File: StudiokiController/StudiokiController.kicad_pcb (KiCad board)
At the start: 2 copper layers, 23 parts, among them J1 USB_B_Mini, J2 Conn_01x30_Male, Q1 Q_DUAL_NPN_NPN_E1B1C2E2B2C1, U1 CH340G, U2 ESP32-WROOM-32D

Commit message: Added MAX31855
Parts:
- added C12: 0.1uF, Capacitor_SMD:C_0603_1608Metric, F.Cu at (124.7, 143.8)
- added J3: Conn_01x04_Male, Connector_PinHeader_2.54mm:PinHeader_1x04_P2.54mm_Vertical, F.Cu at (120.4, 135.8)
- added J4: 57PC5FS, StudiokiController:57PC5FS, F.Cu at (101.3, 144.3)
- added J5: Conn_01x02_Female, TerminalBlock:TerminalBlock_bornier-2_P5.08mm, F.Cu at (125.9, 138.0)
- added R10: 100, Resistor_SMD:R_0603_1608Metric, F.Cu at (128.7, 143.8)
- added R11: 100, Resistor_SMD:R_0603_1608Metric, F.Cu at (128.5, 146.3)
- added R8: 100, Resistor_SMD:R_0603_1608Metric, F.Cu at (136.3, 134.7)
- added R9: 100, Resistor_SMD:R_0603_1608Metric, F.Cu at (120.1, 153.4)
- added U3: MAX31855KASA, Package_SO:SOIC-8_3.9x4.9mm_P1.27mm, F.Cu at (122.3, 148.9)
- U1: value CH340G -> CH340C
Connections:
- J2 pad 14: DISPLAY -> DISP_RES
- U2 pad 13: DISPLAY -> MTMS
- U2 pad 14: Net-(U2-Pad14) -> MTDI
- U2 pad 16: Net-(U2-Pad16) -> MTCK
- U2 pad 18: Net-(U2-Pad18) -> SPI_SCK
- U2 pad 19: Net-(U2-Pad19) -> SPI_MISO
- U2 pad 23: SW1 -> MTDO
- U2 pad 26: Net-(U2-Pad26) -> DISP_RES
- U2 pad 27: SW2 -> Net-(U2-Pad27)
- U2 pad 28: SW3 -> SW1
- U2 pad 29: Net-(U2-Pad29) -> SPI_SS
- U2 pad 30: Net-(U2-Pad30) -> SW2
- U2 pad 31: Net-(U2-Pad31) -> SW3

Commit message: added several Parts
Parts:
- added D1: LED, LED_SMD:LED_0603_1608Metric, F.Cu at (93.5, 106.2)
- added D2: 1N4148W-TP, Diode_SMD:D_SOD-123, F.Cu at (90.5, 105.3)
- added D3: LED, LED_SMD:LED_0603_1608Metric, F.Cu at (89.5, 91.9)
- added D4: 1N4148W-TP, Diode_SMD:D_SOD-123, F.Cu at (90.3, 88.9)
- added F1: Fuse, StudiokiController:Littelfuse65800001009, F.Cu at (108.0, 54.6)
- added J6: Screw_Terminal_01x03, WJ142R-5.08-3P:RHDR6W120P762X508_2X3_1524X1410X1355P, F.Cu at (123.2, 55.9)
- added J7: WJ142R-5.08-3P, StudiokiController:RHDR6W120P762X508_2X3_1524X1410X1355P, F.Cu at (121.9, 83.8)
- added PS1: RAC03-12SK, RAC03-12SK:CONV_RAC03-12SK, F.Cu at (104.1, 71.1)
- added Q2: PMV20XNE, Package_TO_SOT_SMD:SOT-23, F.Cu at (91.1, 100.2)
- added Q3: PMV20XNE, Package_TO_SOT_SMD:SOT-23, F.Cu at (95.4, 89.5)
- added R12: 10k, Resistor_SMD:R_0603_1608Metric, F.Cu at (94.6, 102.2)
- added R13: 10k, Resistor_SMD:R_0603_1608Metric, F.Cu at (93.5, 93.0)
- added RLA1: OJE-SH-112HM_000, StudiokiController:OJE-SH-112HM_000, F.Cu at (100.3, 105.4)
- added RLA2: OJE-SH-112HM_000, StudiokiController:OJE-SH-112HM_000, F.Cu at (100.3, 94.0)
- added SW1: SW_Push, StudiokiController:TSA063G50250, F.Cu at (56.5, 101.0)
- added SW2: SW_Push, StudiokiController:TSA063G50250, F.Cu at (56.5, 109.2)
- added SW3: SW_Push, StudiokiController:TSA063G50250, F.Cu at (56.5, 92.7)
- moved J1 78.8 mm to (63.8, 53.9), turned to 180 degrees
- moved J5 55.7 mm to (79.2, 107.7), turned to 180 degrees
- moved U1 53.4 mm to (74.9, 57.8)
- moved U2 45.1 mm to (65.4, 74.9), turned to 90 degrees
- moved C1 43.3 mm to (161.5, 68.8)
- moved C4 43.3 mm to (161.5, 66.3)
- moved C5 43.3 mm to (165.6, 63.8)
- moved R1 43.3 mm to (163.8, 77.0)
- moved R2 43.3 mm to (157.1, 72.8)
- moved R3 43.3 mm to (161.5, 63.8)
- moved R4 43.3 mm to (165.6, 61.3)
- moved R6 43.3 mm to (161.5, 61.3)
- moved C2 43.3 mm to (153.1, 72.8)
- moved C3 43.3 mm to (153.1, 77.8)
- moved R5 43.3 mm to (153.1, 75.3)
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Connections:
- U2 pad 11: Net-(U2-Pad11) -> RELAY1
- U2 pad 12: Net-(U2-Pad12) -> RELAY2
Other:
- board outline added: 85 x 65 mm

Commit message: first PCB
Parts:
- removed R10, R11, R9: 100, Resistor_SMD:R_0603_1608Metric
- added C10: 100nF, Capacitor_SMD:C_0603_1608Metric, F.Cu at (58.3, 62.9)
- added C13: 100nF, Capacitor_SMD:C_0603_1608Metric, F.Cu at (61.4, 118.4)
- added C19: 1uF, Capacitor_SMD:C_0603_1608Metric, F.Cu at (56.9, 99.2)
- added C6: 100nF, Capacitor_SMD:C_0603_1608Metric, F.Cu at (58.6, 97.2)
- added C7: 100nF, Capacitor_SMD:C_0603_1608Metric, F.Cu at (93.0, 70.4)
- added C8: 10uF tantal, Capacitor_Tantalum_SMD:CP_EIA-3216-12_Kemet-S, F.Cu at (92.5, 72.6)
- added C9: 10uF tantal, Capacitor_Tantalum_SMD:CP_EIA-3216-12_Kemet-S, F.Cu at (87.1, 66.3)
- added D5: LED, LED_SMD:LED_0603_1608Metric, F.Cu at (66.7, 87.7)
- added D6: LED, LED_SMD:LED_0603_1608Metric, F.Cu at (68.5, 87.7)
- added D7: LED, LED_SMD:LED_0603_1608Metric, F.Cu at (64.9, 87.7)
- added D8: LED, LED_SMD:LED_0603_1608Metric, F.Cu at (97.6, 117.2)
- added D9: 1N4148W-TP, Diode_SMD:D_SOD-123, F.Cu at (105.7, 115.5)
- added J2: WJ142R-5.08-3P, StudiokiController:RHDR6W120P762X508_2X3_1524X1410X1355P, F.Cu at (137.2, 105.7)
- added J8: Conn_01x04_Female, Connector_PinHeader_2.54mm:PinHeader_1x04_P2.54mm_Vertical, F.Cu at (65.9, 96.4)
- added J9: Conn_01x04_Female, Connector_PinHeader_2.54mm:PinHeader_1x04_P2.54mm_Vertical, F.Cu at (61.2, 96.4)
- added Q4: PMV20XNE, Package_TO_SOT_SMD:SOT-23, F.Cu at (102.2, 117.2)
- added RLA3: OJE-SH-112HM_000, StudiokiController:OJE-SH-112HM_000, F.Cu at (108.7, 118.9)
- added U4: AZ1117-3.3, Package_TO_SOT_SMD:SOT-223, F.Cu at (91.9, 64.5)
- C11: value 1uF -> 100nF
- C12: value 0.1uF -> 100nF
- J3: value Conn_01x04_Male -> Conn_01x04_Female
- J6: value Screw_Terminal_01x03 -> WJ142R-5.08-3P; footprint WJ142R-5.08-3P:RHDR6W120P762X508_2X3_1524X1410X1355P -> StudiokiController:RHDR6W120P762X508_2X3_1524X1410X1355P
- R8: value 100 -> 10k
- SW1, SW2, SW3: footprint StudiokiController:TSA063G50250 -> Button_Switch_SMD:SW_SPST_PTS645
- moved C5 109.5 mm to (58.8, 88.0), turned to 180 degrees
- moved C11 105.6 mm to (54.3, 118.5), turned to 180 degrees
- moved C15 105.5 mm to (55.8, 109.9)
- moved C14 105.3 mm to (55.8, 111.5)
- moved C4 104.7 mm to (58.8, 86.2), turned to 180 degrees
- moved R3 99.9 mm to (61.6, 63.5), turned to 90 degrees
- moved C16 98.9 mm to (55.7, 96.0), turned to 180 degrees
- moved C2 95.9 mm to (58.8, 89.7), turned to 180 degrees
- moved C18 95.6 mm to (55.3, 99.2), turned to 270 degrees
- moved C17 95.1 mm to (55.5, 92.7), turned to 180 degrees
- moved R2 94.3 mm to (63.3, 63.5), turned to 90 degrees
- moved C1 90.9 mm to (71.5, 56.2)
- moved R4 87.5 mm to (78.1, 57.7), turned to 270 degrees
- moved R1 84.7 mm to (80.8, 60.5)
- moved R6 82.9 mm to (78.8, 66.3)
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- renumbered C6 to C14, C7 to C15, C8 to C16, C9 to C17, C10 to C18, J2 to J10
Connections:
- C11 pad 1: +3V3 -> GND
- C11 pad 2: Net-(C10-Pad2) -> SW2
- C18 pad 2: Net-(C10-Pad2) -> GND
- D2 pad 1: Net-(D2-Pad1) -> +12V
- D4 pad 1: Net-(D4-Pad1) -> +12V
- J3 pad 1: Net-(J3-Pad1) -> GND
- J3 pad 2: Net-(J3-Pad2) -> +3V3
- J3 pad 3: Net-(J3-Pad3) -> SCL
- J3 pad 4: Net-(J3-Pad4) -> SDA
- J5 pad 1: Net-(J4-Pad1) -> Net-(J4-Pad3)
- J5 pad 2: Net-(J4-Pad2) -> Net-(J4-Pad1)
- J6 pad 1: Net-(J6-Pad1) -> Net-(F1-Pad2)
- J6 pad 2: 230V-N -> Net-(F1-Pad2)
- J6 pad 3: Net-(F1-Pad2) -> 230V-N
- J6 pad 4: (no net) -> 230V-N
- J6 pad 5: (no net) -> PE
- J6 pad 6: (no net) -> PE
- J7 pad 2: Net-(J7-Pad2) -> 230V-N
- J7 pad 4: Net-(J7-Pad4) -> /230V-Relay/OUTPUT-A
- J7 pad 5: Net-(J7-Pad5) -> PE
- J7 pad 6: Net-(J7-Pad6) -> PE
- R8 pad 1: MTMS -> RELAY3
- R8 pad 2: Net-(J3-Pad1) -> GND
- U2 pad 1: Net-(U2-Pad1) -> GND
- U2 pad 10: Net-(U2-Pad10) -> RELAY3
- U2 pad 13: MTMS -> Net-(U2-Pad13)
- U2 pad 14: MTDI -> Net-(U2-Pad14)
- U2 pad 15: Net-(U2-Pad1) -> GND
- U2 pad 16: MTCK -> SCL
- U2 pad 17: Net-(U2-Pad17) -> SDA
- U2 pad 23: MTDO -> Net-(U2-Pad23)
- U2 pad 28: SW1 -> Net-(U2-Pad28)
- U2 pad 36: SCL -> Net-(U2-Pad36)
- U2 pad 37: SDA -> SW1
- U2 pad 38: Net-(U2-Pad1) -> GND
- U2 pad 7: Net-(U2-Pad7) -> LED3
- U2 pad 8: Net-(U2-Pad8) -> LED1
- U2 pad 9: Net-(U2-Pad9) -> LED2
- U3 pad 2: Net-(J4-Pad1) -> Net-(J4-Pad3)
- U3 pad 3: Net-(J4-Pad2) -> Net-(J4-Pad1)
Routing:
- net +3V3: track 0.00 -> 137.3 mm, vias 0 -> 4
- net 230V-N: track 0.00 -> 75.7 mm
- net +12V: track 0.00 -> 74.8 mm
- net PE: track 0.00 -> 73.1 mm
- net SW2: track 0.00 -> 71.8 mm, vias 0 -> 2
- net 230V-L: track 0.00 -> 70.6 mm
- net GND: track 0.00 -> 65.4 mm, vias 0 -> 18
- net SW3: track 0.00 -> 65.3 mm, vias 0 -> 2
- net RELAY3: track 0.00 -> 59.7 mm
- net SPI_SS: track 0.00 -> 51.6 mm, vias 0 -> 2
- net SDA: track 0.00 -> 50.8 mm, vias 0 -> 2
- net DISP_RES: track 0.00 -> 49.2 mm, vias 0 -> 2
- net EN: track 0.00 -> 48.7 mm, vias 0 -> 2
- net SCL: track 0.00 -> 46.6 mm, vias 0 -> 2
- net RELAY1: track 0.00 -> 46.5 mm
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- added copper zone on B.Cu, net GND
- added copper zone on F.Cu, net GND
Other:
- board size 85 x 65 mm -> 100 x 80 mm
- board text added: "PE"

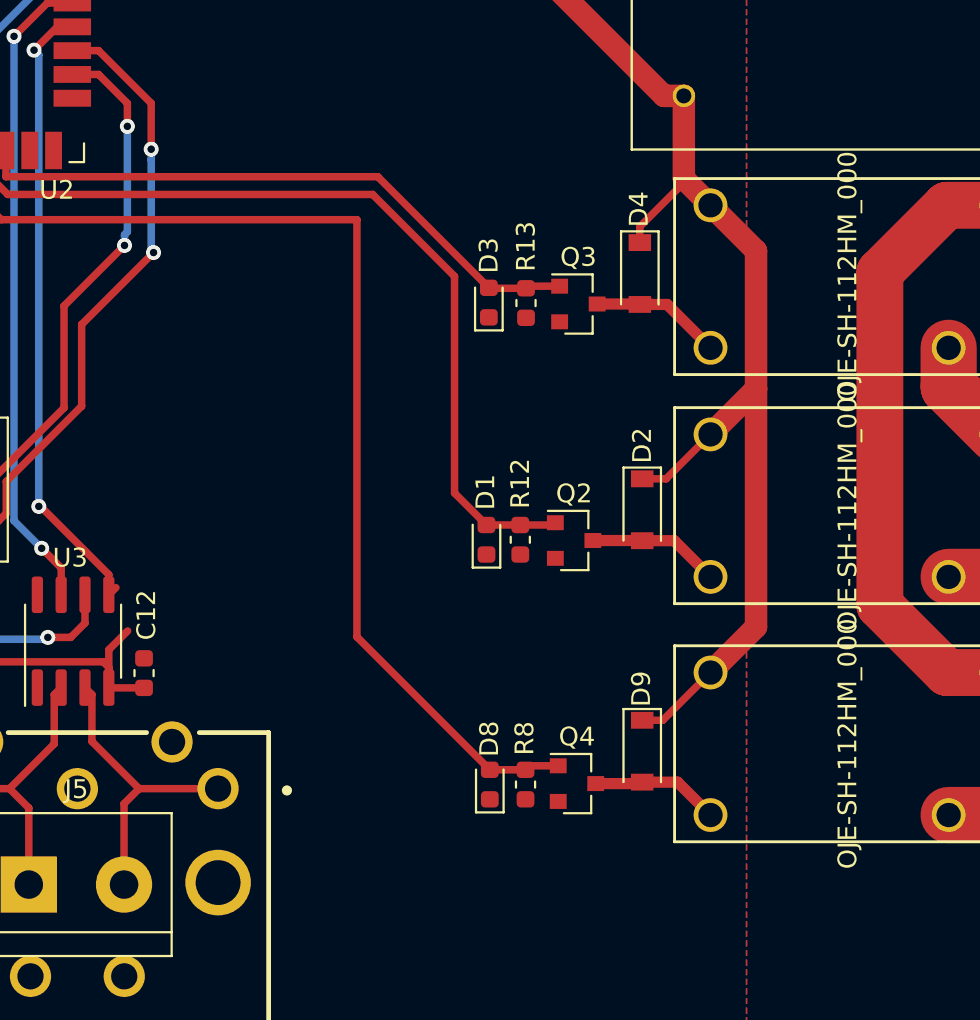
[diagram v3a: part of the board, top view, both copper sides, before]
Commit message: changed silkscreen
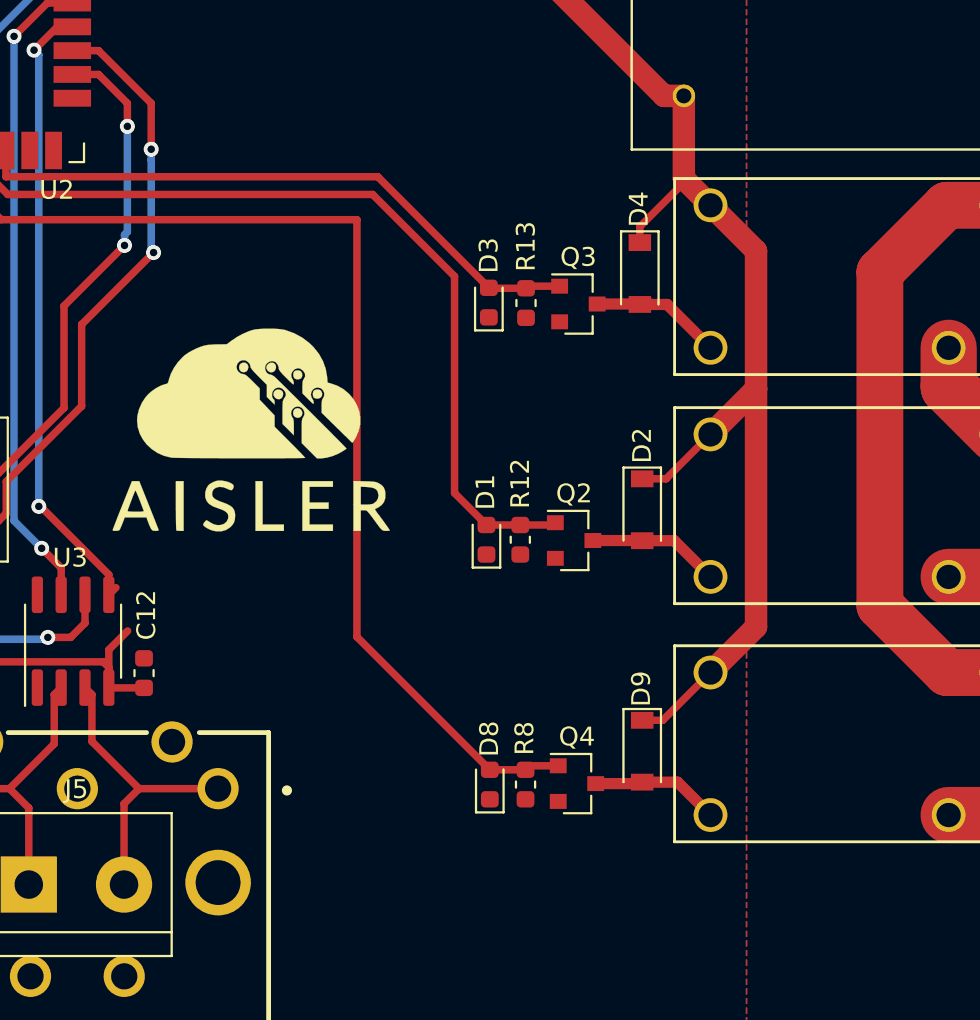
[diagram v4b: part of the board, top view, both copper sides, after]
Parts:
- added G***: LOGO, StudiokiController:Aisler_Logo, F.Cu at (84.8, 98.3)

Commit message: New Layout
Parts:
- removed C14: 2.2uF, Capacitor_SMD:C_0603_1608Metric
- removed C15: 4.7uF, Capacitor_SMD:C_0603_1608Metric
- removed C16, C17, C18, C19: 1uF, Capacitor_SMD:C_0603_1608Metric
- added H1: MountingHole, MountingHole:MountingHole_3.2mm_M3_Pad_Via, F.Cu at (186.8, 66.4)
- added H2: MountingHole, MountingHole:MountingHole_3.2mm_M3_Pad_Via, F.Cu at (186.8, 115.7)
- added H3: MountingHole, MountingHole:MountingHole_3.2mm_M3_Pad_Via, F.Cu at (267.3, 66.4)
- added H4: MountingHole, MountingHole:MountingHole_3.2mm_M3_Pad_Via, F.Cu at (267.3, 115.7)
- added J11: Screw_Terminal_01x03, TerminalBlock_Phoenix:TerminalBlock_Phoenix_PT-1,5-3-5.0-H_1x03_P5.00mm_Horizontal, F.Cu at (244.6, 53.3)
- added J12: Screw_Terminal_01x02, TerminalBlock_Phoenix:TerminalBlock_Phoenix_PT-1,5-2-5.0-H_1x02_P5.00mm_Horizontal, F.Cu at (264.6, 53.3)
- added R10: 100, Resistor_SMD:R_0603_1608Metric, F.Cu at (245.7, 118.8)
- added R9: 100, Resistor_SMD:R_0603_1608Metric, F.Cu at (245.7, 115.3)
- added RV1: MOV-07D391KTR, Varistor:RV_Disc_D7mm_W4.5mm_P5mm, F.Cu at (199.4, 66.0)
- J10: value Conn_01x30_Male -> Conn_01x10_Male; footprint StudiokiController:OLED-solder -> Connector_IDC:IDC-Header_2x05_P2.54mm_Vertical
- J2, J6, J7: value WJ142R-5.08-3P -> Screw_Terminal_01x03; footprint StudiokiController:RHDR6W120P762X508_2X3_1524X1410X1355P -> TerminalBlock_Phoenix:TerminalBlock_Phoenix_PT-1,5-3-5.0-H_1x03_P5.00mm_Horizontal
- J3, J8, J9: footprint Connector_PinHeader_2.54mm:PinHeader_1x04_P2.54mm_Vertical -> Connector_PinSocket_2.54mm:PinSocket_1x04_P2.54mm_Vertical
- R7: value 910K -> 100
- moved J4 203.4 mm to (276.9, 101.2), turned to 180 degrees
- moved C6 197.3 mm to (253.6, 127.6), turned to 180 degrees
- moved J5 197.2 mm to (269.3, 103.8), turned to 90 degrees
- moved J9 193.7 mm to (252.8, 125.0), turned to 90 degrees
- moved R7 190.1 mm to (245.7, 117.0), turned to 180 degrees
- moved J8 188.4 mm to (252.8, 119.9), turned to 90 degrees
- moved C5 187.0 mm to (242.0, 125.3), turned to 270 degrees
- moved C4 185.6 mm to (240.2, 125.3), turned to 270 degrees
- moved C2 184.3 mm to (240.2, 122.0), turned to 90 degrees
- moved J3 183.2 mm to (252.8, 114.8), turned to 90 degrees
- moved U3 181.1 mm to (256.3, 101.4), turned to 180 degrees
- moved D7 180.3 mm to (242.5, 118.8), turned to 180 degrees
- moved C12 179.4 mm to (258.0, 97.6), turned to 180 degrees
- moved D5 178.2 mm to (242.5, 117.0), turned to 180 degrees
- moved D6 176.2 mm to (242.5, 115.2), turned to 180 degrees
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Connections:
- D5 pad 1: GND -> Net-(D5-Pad1)
- D6 pad 1: GND -> Net-(D6-Pad1)
- D7 pad 1: GND -> Net-(D7-Pad1)
- J10 pad 1: GND -> +3V3
- J10 pad 10: GND -> SW3
- J10 pad 2: Net-(C17-Pad2) -> EN
- J10 pad 3: Net-(C17-Pad1) -> IO0
- J10 pad 4: Net-(C16-Pad1) -> IO2
- J10 pad 5: Net-(C16-Pad2) -> SCL
- J10 pad 6: +3V3 -> SDA
- J10 pad 7: Net-(J10-Pad7) -> SW1
- J10 pad 8: GND -> SW2
- J10 pad 9: +3V3 -> GND
- J2 pad 1: 230V-N -> PE
- J2 pad 2: 230V-N -> Net-(F1-Pad2)
- J2 pad 3: /sheet5DF376A8/OUTPUT-A -> 230V-N
- J6 pad 1: Net-(F1-Pad2) -> Net-(J6-Pad1)
- J6 pad 2: Net-(F1-Pad2) -> /230V-Relay/OUTPUT-B
- J6 pad 3: 230V-N -> /230V-Relay/OUTPUT-A
- J7 pad 1: 230V-N -> Net-(J7-Pad1)
- J7 pad 2: 230V-N -> /sheet5DF55D65/OUTPUT-B
- J7 pad 3: /230V-Relay/OUTPUT-A -> /sheet5DF55D65/OUTPUT-A
- R7 pad 1: Net-(J10-Pad26) -> GND
- R7 pad 2: GND -> Net-(D5-Pad1)
- RLA1 pad 1: /sheet5DF55D65/OUTPUT-A -> /230V-Relay/OUTPUT-B
- RLA2 pad 1: 230V-L -> /sheet5DF55D65/OUTPUT-B
- RLA3 pad 1: 230V-L -> /sheet5DF376A8/OUTPUT-B
- U2 pad 11: RELAY1 -> RELAY2
- U2 pad 12: RELAY2 -> RELAY1
- U2 pad 14: Net-(U2-Pad14) -> DOOR
- U2 pad 24: Net-(U2-Pad24) -> IO2
- U2 pad 26: DISP_RES -> SW1
- U2 pad 27: Net-(U2-Pad27) -> SW2
- U2 pad 28: Net-(U2-Pad28) -> SW3
- U2 pad 30: SW2 -> Net-(U2-Pad30)
- U2 pad 31: SW3 -> Net-(U2-Pad31)
- U2 pad 37: SW1 -> Net-(U2-Pad37)
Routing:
- net DOOR: track 0.00 -> 77.1 mm, vias 0 -> 2
- net PE: track 73.1 -> 0.00 mm
- net 230V-L: track 70.6 -> 8.20 mm
- net SW1: track 15.6 -> 74.7 mm, vias 0 -> 1
- net 230V-N: track 75.7 -> 23.2 mm
- net DISP_RES: track 49.2 -> 0.00 mm, vias 2 -> 0
- net GND: track 65.4 -> 24.1 mm, vias 18 -> 12
- net +12V: track 74.8 -> 100.5 mm
- net SCL: track 46.6 -> 67.9 mm, vias 2 -> 1
- net SDA: track 50.8 -> 71.4 mm, vias 2 -> 1
- net /230V-Relay/OUTPUT-A: track 33.5 -> 13.9 mm
- net IO2: track 0.00 -> 15.5 mm
- net RELAY3: track 59.7 -> 45.4 mm, vias 0 -> 2
- net +3V3: track 137.3 -> 123.5 mm, vias 4 -> 6
- net IO0: track 13.6 -> 26.8 mm, vias 0 -> 2
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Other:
- board size 100 x 80 mm -> 100 x 85 mm
- board text added: "3V3"
- board text added: "EN"
- board text added: "GND"
- board text added: "IO0"
- board text added: "IO2"
- board text added: "Jan² 12-2019"
- board text added: "L"
- board text added: "N"
- board text added: "SCL"
- board text added: "SDA"
- board text added: "SW1"
- board text added: "SW2"
- board text added: "SW3"
- board text added: "Studioki Controll"

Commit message: changed parameters
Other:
- net class Default: clearance 0.2 -> 0.15
- rule pad_to_mask_clearance: 0.051 -> 0.02
- rule solder_mask_min_width: 0.25 -> 0.2
- rule trace_clearance: 0.2 -> 0.15
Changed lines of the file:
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@@
   )
   (setup
-    (last_trace_width 2)
+    (last_trace_width 0.4)
     (user_trace_width 0.4)
     (user_trace_width 0.8)
@@
     (user_trace_width 2)
     (user_trace_width 3)
-    (trace_clearance 0.2)
+    (trace_clearance 0.15)
     (zone_clearance 0.508)
     (zone_45_only no)
@@
     (pad_size 1.524 1.524)
     (pad_drill 0.762)
-    (pad_to_mask_clearance 0.051)
-    (solder_mask_min_width 0.25)
+    (pad_to_mask_clearance 0.02)
+    (solder_mask_min_width 0.2)
     (aux_axis_origin 0 0)
     (visible_elements 7FFFFFFF)
@@
   (net 79 "Net-(J11-Pad1)")
   (net_class Default "This is the default net class."
-    (clearance 0.2)
+    (clearance 0.15)
     (trace_width 0.25)
     (via_dia 0.8)
